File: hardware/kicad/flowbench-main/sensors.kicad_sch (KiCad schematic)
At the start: 37 parts, among them J9 BME280 (GX12-4), U2 TCA9548APWR, U3 ABP2DRRN100MD2A3XX, U4 ABP2DRRN100MD2A3XX, U5 ABP2DRRN100MD2A3XX, U6 ADS1219 #1 (0x40), U7 ADS1219 #2 (0x41)

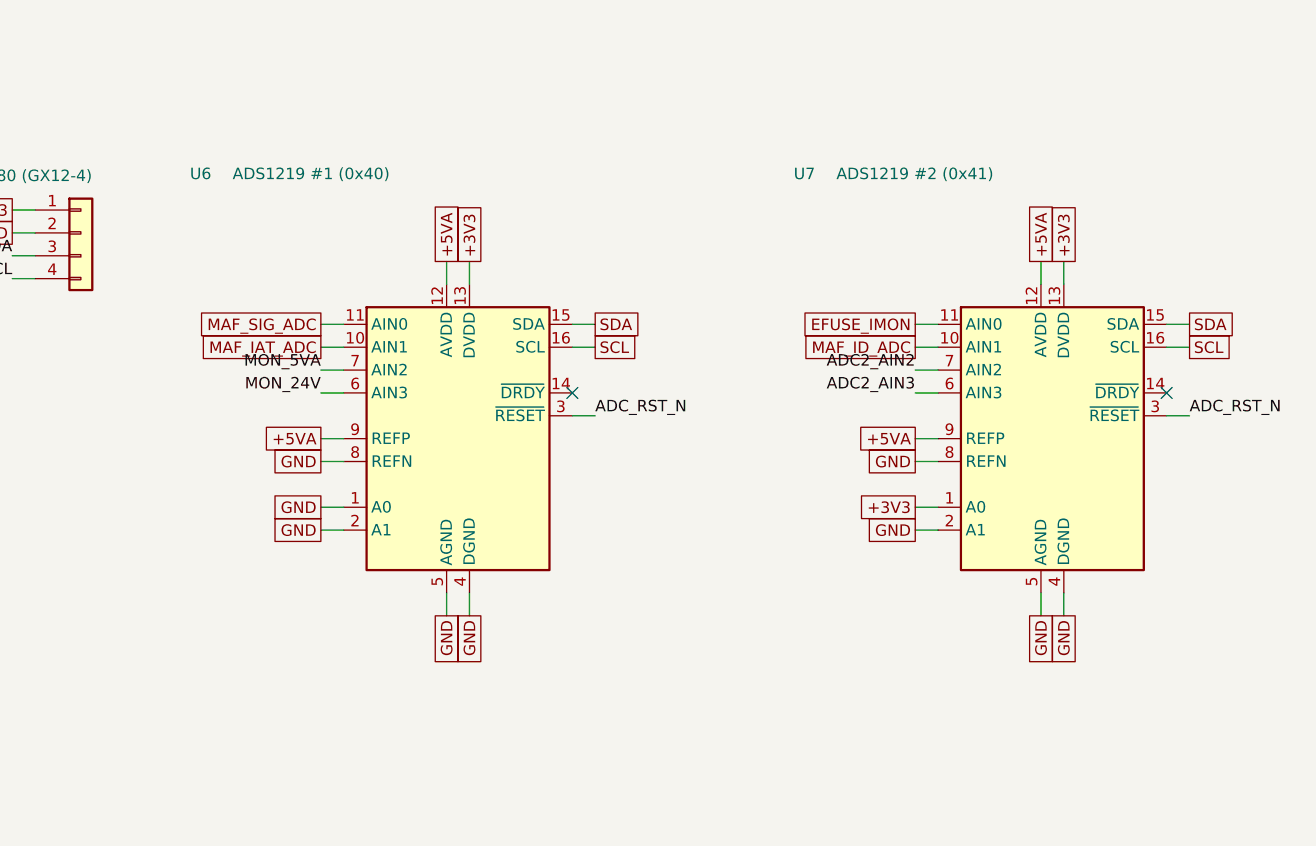
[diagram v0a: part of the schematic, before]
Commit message: KiCad: fix off-grid pins on ADS1219 and AM26C31 symbols
A floating-point modulo misread the symbol half-height as off-grid and
shifted it by half a step, leaving top and bottom pins 0.635 mm off the
1.27 mm connection grid (16 ERC warnings). verify.py now checks every pin
and wire end against the grid.

Co-Authored-By: Claude Opus 5.5 <noreply@anthropic.com>
Claude-Session: https://claude.ai/code/session_01QEmmugJA9S77dSDSNcKrPa
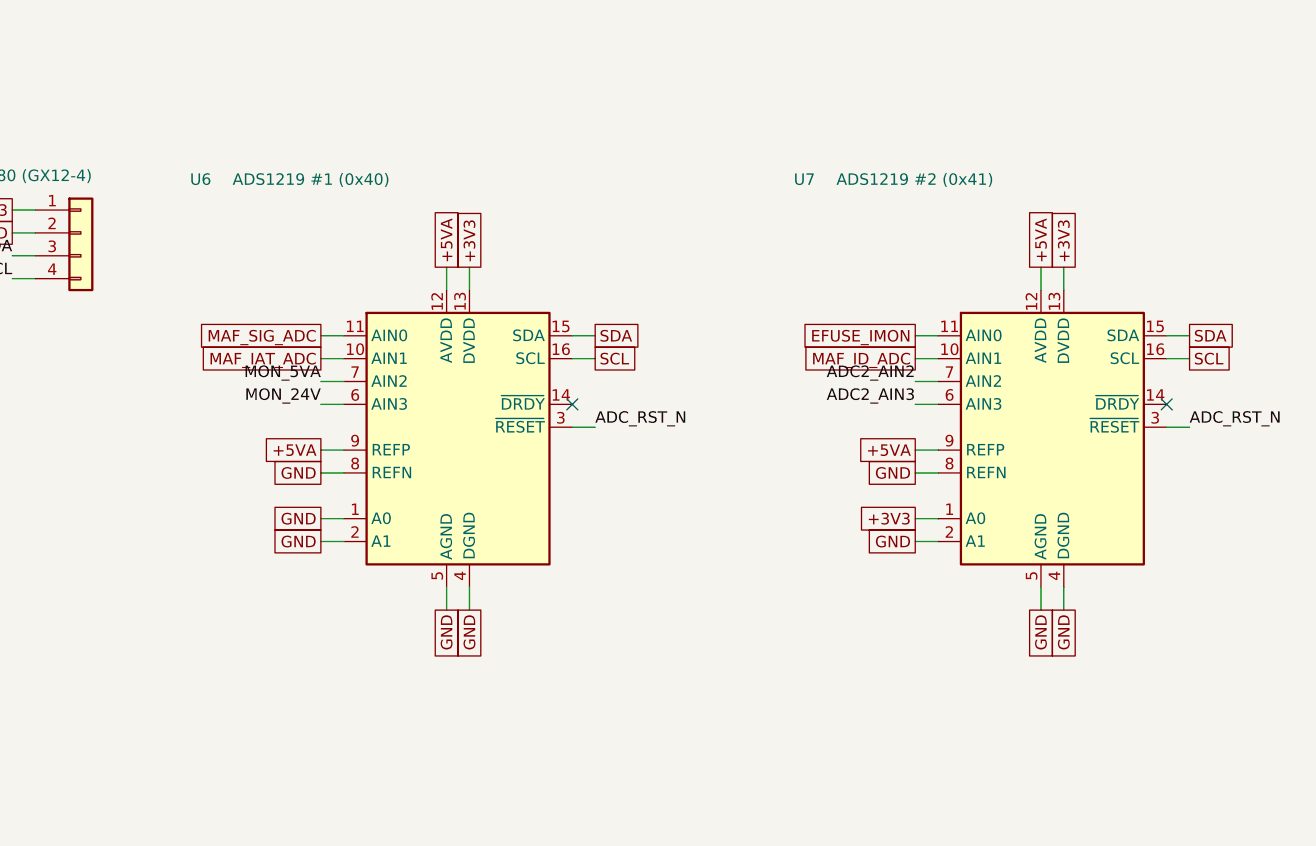
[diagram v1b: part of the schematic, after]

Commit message: KiCad: WIZ850io as one part with a two-row footprint
Pinout and size confirmed from the module (20 x 25 mm, two 1x6 headers).
The two header symbols become one 12-pin WIZ850io part on footprint
FlowBench:WIZ850io (J1 pads 1-6, J2 pads 7-12, rows 17.78 mm apart), so the
headers can't be placed at the wrong spacing.

Co-Authored-By: Claude Opus 5.5 <noreply@anthropic.com>
Claude-Session: https://claude.ai/code/session_01QEmmugJA9S77dSDSNcKrPa
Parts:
- removed J9: BME280 (GX12-4), Connector_Phoenix_MC:PhoenixContact_MC_1,5_4-G-3.81_1x04_P3.81mm_Horizontal, symbol FlowBench:Conn_01x04
- removed U2: TCA9548APWR, Package_SO:TSSOP-24_4.4x7.8mm_P0.65mm, symbol FlowBench:TCA9548APWR
- removed U3: ABP2DRRN100MD2A3XX, symbol FlowBench:ABP2_I2C
- removed U6: ADS1219 #1 (0x40), Package_SO:TSSOP-16_4.4x5mm_P0.65mm, symbol FlowBench:ADS1219
- added J7: BME280 (GX12-4), Connector_Phoenix_MC:PhoenixContact_MC_1,5_4-G-3.81_1x04_P3.81mm_Horizontal, symbol FlowBench:Conn_01x04
- added U3: TCA9548APWR, Package_SO:TSSOP-24_4.4x7.8mm_P0.65mm, symbol FlowBench:TCA9548APWR
- added U6: ABP2DRRN100MD2A3XX, symbol FlowBench:ABP2_I2C
- added U8: ADS1219 #2 (0x41), Package_SO:TSSOP-16_4.4x5mm_P0.65mm, symbol FlowBench:ADS1219
- U4: Function Orifice pressure -> Reference pressure
- U5: Function Pitot pressure -> Orifice pressure
- U7: value ADS1219 #2 (0x41) -> ADS1219 #1 (0x40)
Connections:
- net +3V3: now also J7.1 (Pin_1), U3.24 (VCC), U6.1 (VDD), U8.1 (A0), U8.13 (DVDD); no longer U7.1 (A0)
- net +5VA: now also U8.12 (AVDD), U8.9 (REFP)
- net ADC2_AIN2: now also U8.7 (AIN2); no longer U7.7 (AIN2)
- net ADC2_AIN3: now also U8.6 (AIN3); no longer U7.6 (AIN3)
- net ADC_RST_N: now also U8.3 (~{RESET})
- net EFUSE_IMON: now also U8.11 (AIN0); no longer U7.11 (AIN0)
- net GND: now also U7.1 (A0), J7.2 (Pin_2), U3.1 (A0), U3.12 (GND), U3.2 (A1), U3.21 (A2), U6.5 (GND), U8.2 (A1), U8.4 (DGND), U8.5 (AGND), U8.8 (REFN)
- net MAF_IAT_ADC: now also U7.10 (AIN1)
- net MAF_ID_ADC: now also U8.10 (AIN1); no longer U7.10 (AIN1)
- net MAF_SIG_ADC: now also U7.11 (AIN0)
- net MON_24V: now also U7.6 (AIN3)
- net MON_5VA: now also U7.7 (AIN2)
- net MUX0_SCL: now also U4.2 (SCL), U3.5 (SC0)
- net MUX0_SDA: now also U4.4 (SDA), U3.4 (SD0)
- net MUX1_SCL: now also U5.2 (SCL), U3.7 (SC1); no longer U4.2 (SCL)
- net MUX1_SDA: now also U5.4 (SDA), U3.6 (SD1); no longer U4.4 (SDA)
- net MUX2_SCL: now also U3.9 (SC2), U6.2 (SCL); no longer U5.2 (SCL)
- net MUX2_SDA: now also U3.8 (SD2), U6.4 (SDA); no longer U5.4 (SDA)
- net MUX3_SCL: now also J7.4 (Pin_4), U3.11 (SC3)
- net MUX3_SDA: now also J7.3 (Pin_3), U3.10 (SD3)
- net MUX_RST_N: now also U3.3 (~{RESET})
- net SCL: now also U3.22 (SCL), U8.16 (SCL)
- net SDA: now also U3.23 (SDA), U8.15 (SDA)

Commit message: KiCad: DevKit as one part with a 25.4 mm two-row footprint
Header pinout confirmed against Espressif's J1/J3 tables; row spacing measured
at 25.4 mm. The two header symbols become one 44-pin ESP32-S3-DevKitC-1 part on
footprint FlowBench:ESP32-S3-DevKitC-1 (J1 pads 1-22, J3 pads 23-44), with the
antenna end marked. BOM notes the N32R16V as a drop-in alternative.

Co-Authored-By: Claude Opus 5.5 <noreply@anthropic.com>
Claude-Session: https://claude.ai/code/session_01QEmmugJA9S77dSDSNcKrPa
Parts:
- removed J7: BME280 (GX12-4), Connector_Phoenix_MC:PhoenixContact_MC_1,5_4-G-3.81_1x04_P3.81mm_Horizontal, symbol FlowBench:Conn_01x04
- removed U3: TCA9548APWR, Package_SO:TSSOP-24_4.4x7.8mm_P0.65mm, symbol FlowBench:TCA9548APWR
- removed U4: ABP2DRRN100MD2A3XX, symbol FlowBench:ABP2_I2C
- removed U7: ADS1219 #1 (0x40), Package_SO:TSSOP-16_4.4x5mm_P0.65mm, symbol FlowBench:ADS1219
- added J5: BME280 (GX12-4), Connector_Phoenix_MC:PhoenixContact_MC_1,5_4-G-3.81_1x04_P3.81mm_Horizontal, symbol FlowBench:Conn_01x04
- added U4: TCA9548APWR, Package_SO:TSSOP-24_4.4x7.8mm_P0.65mm, symbol FlowBench:TCA9548APWR
- added U7: ABP2DRRN100MD2A3XX, symbol FlowBench:ABP2_I2C
- added U9: ADS1219 #2 (0x41), Package_SO:TSSOP-16_4.4x5mm_P0.65mm, symbol FlowBench:ADS1219
- U5: Function Orifice pressure -> Reference pressure
- U6: Function Pitot pressure -> Orifice pressure
- U8: value ADS1219 #2 (0x41) -> ADS1219 #1 (0x40)
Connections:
- net +3V3: now also J5.1 (Pin_1), U4.24 (VCC), U7.1 (VDD), U9.1 (A0), U9.13 (DVDD); no longer U8.1 (A0)
- net +5VA: now also U9.12 (AVDD), U9.9 (REFP)
- net ADC2_AIN2: now also U9.7 (AIN2); no longer U8.7 (AIN2)
- net ADC2_AIN3: now also U9.6 (AIN3); no longer U8.6 (AIN3)
- net ADC_RST_N: now also U9.3 (~{RESET})
- net EFUSE_IMON: now also U9.11 (AIN0); no longer U8.11 (AIN0)
- net GND: now also U8.1 (A0), J5.2 (Pin_2), U4.1 (A0), U4.12 (GND), U4.2 (A1), U4.21 (A2), U7.5 (GND), U9.2 (A1), U9.4 (DGND), U9.5 (AGND), U9.8 (REFN)
- net MAF_IAT_ADC: now also U8.10 (AIN1)
- net MAF_ID_ADC: now also U9.10 (AIN1); no longer U8.10 (AIN1)
- net MAF_SIG_ADC: now also U8.11 (AIN0)
- net MON_24V: now also U8.6 (AIN3)
- net MON_5VA: now also U8.7 (AIN2)
- net MUX0_SCL: now also U5.2 (SCL), U4.5 (SC0)
- net MUX0_SDA: now also U5.4 (SDA), U4.4 (SD0)
- net MUX1_SCL: now also U6.2 (SCL), U4.7 (SC1); no longer U5.2 (SCL)
- net MUX1_SDA: now also U6.4 (SDA), U4.6 (SD1); no longer U5.4 (SDA)
- net MUX2_SCL: now also U4.9 (SC2), U7.2 (SCL); no longer U6.2 (SCL)
- net MUX2_SDA: now also U4.8 (SD2), U7.4 (SDA); no longer U6.4 (SDA)
- net MUX3_SCL: now also J5.4 (Pin_4), U4.11 (SC3)
- net MUX3_SDA: now also J5.3 (Pin_3), U4.10 (SD3)
- net MUX_RST_N: now also U4.3 (~{RESET})
- net SCL: now also U4.22 (SCL), U9.16 (SCL)
- net SDA: now also U4.23 (SDA), U9.15 (SDA)

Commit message: KiCad: correct ABP2 pinout and add its DIP footprint
The ABP2 symbol used a breakout-board pin table. Honeywell datasheet 32350268,
Table 21, gives the sensor's I2C pinout as 1 GND, 2 VDD, 3 EOC, 4 NC, 5 SDA,
6 SCL; the old symbol would have put 3.3 V on GND. Symbol and nets corrected.
New footprint FlowBench:Honeywell_ABP2_DIP from Figure 13 (2.54 mm pitch,
rows 11.00 mm, 0.73 mm holes), with the port side marked.

Co-Authored-By: Claude Opus 5.5 <noreply@anthropic.com>
Claude-Session: https://claude.ai/code/session_01QEmmugJA9S77dSDSNcKrPa
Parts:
- U5, U6, U7: footprint (none) -> FlowBench:Honeywell_ABP2_DIP
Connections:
- net +3V3: now also U5.2 (VDD), U6.2 (VDD), U7.2 (VDD); no longer U5.1 (VDD), U6.1 (VDD), U7.1 (VDD)
- net GND: now also U5.1 (GND), U6.1 (GND), U7.1 (GND); no longer U5.5 (GND), U6.5 (GND), U7.5 (GND)
- net MUX0_SCL: now also U5.6 (SCL); no longer U5.2 (SCL)
- net MUX0_SDA: now also U5.5 (SDA); no longer U5.4 (SDA)
- net MUX1_SCL: now also U6.6 (SCL); no longer U6.2 (SCL)
- net MUX1_SDA: now also U6.5 (SDA); no longer U6.4 (SDA)
- net MUX2_SCL: now also U7.6 (SCL); no longer U7.2 (SCL)
- net MUX2_SDA: now also U7.5 (SDA); no longer U7.4 (SDA)
